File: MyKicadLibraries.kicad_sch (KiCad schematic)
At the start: 18 parts, among them J1 Conn_01x08, J2 Conn_01x08, J3 POGO Pins, J4 c8-inlet, J5 FTDI, SW1 Schurter Switch, U1 radio-receiver, U10 rdm-6300, U2 TP4056, U3 LilygoSIMT7000G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

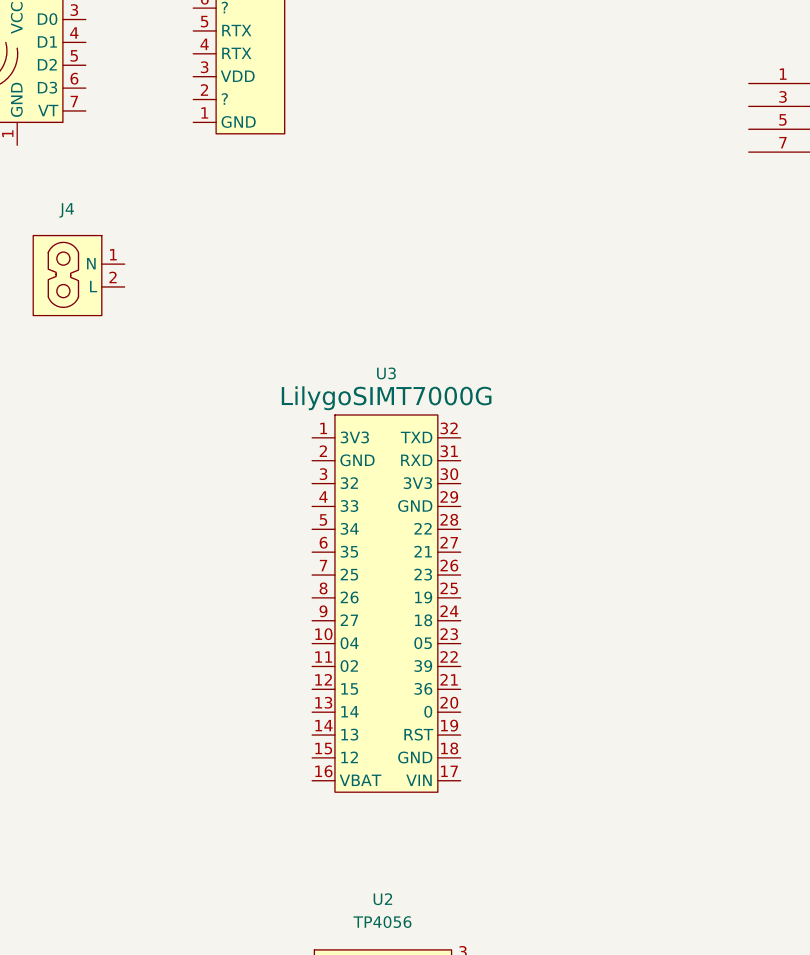
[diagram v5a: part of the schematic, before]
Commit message: add round magnetic charger and update the libraries
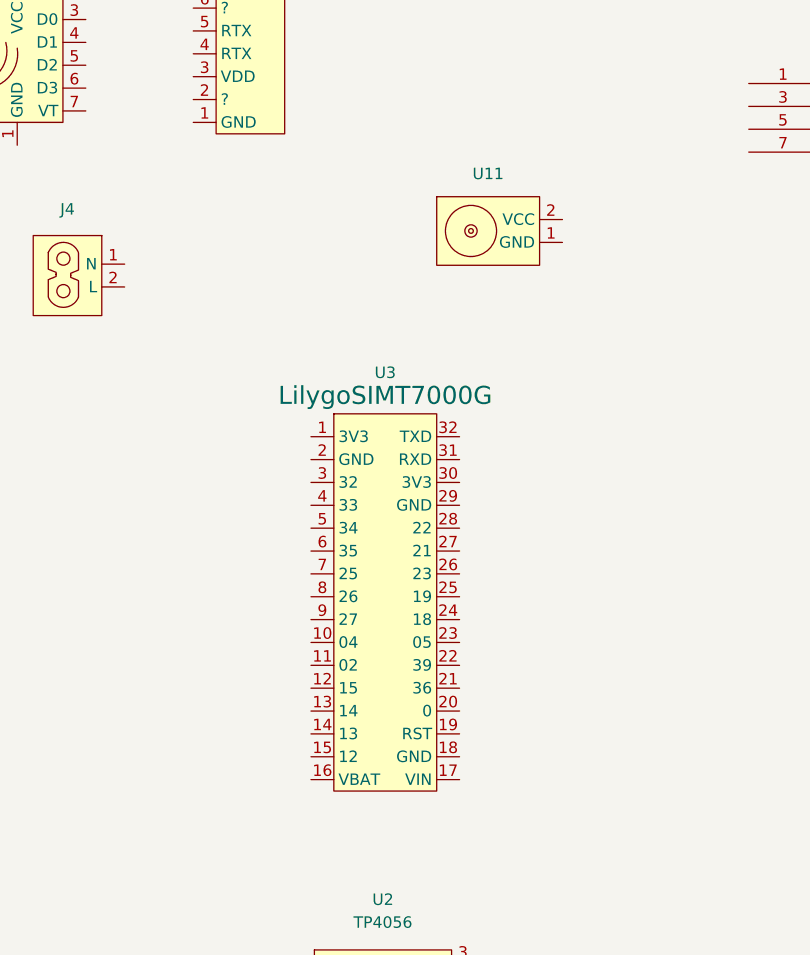
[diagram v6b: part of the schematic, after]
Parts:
- added U11: magnetic-charger, magnetic-charger:magnetic-charger, symbol magnetic-charger:magnetic-charger
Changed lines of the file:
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@@
+    (pin "2")
+  )
+  (symbol (lib_name "magnetic-charger_1") (lib_id "magnetic-charger:magnetic-charger") (at 141.605 71.755 0) (unit 1)
+    (in_bom yes) (on_board yes) (fields_autoplaced)
+    (property "Reference" "U11" (id 0) (at 140.97 65.405 0))
+    (property "Value" "magnetic-charger" (id 1) (at 140.97 76.835 0)
+      (effects (font (size 1.27 1.27)) hide)
+    )
+    (property "Footprint" "magnetic-charger:magnetic-charger" (id 2) (at 145.415 80.01 0)
+      (effects (font (size 1.27 1.27)) hide)
+    )
+    (property "Datasheet" "" (id 3) (at 146.685 72.39 0)
+      (effects (font (size 1.27 1.27)) hide)
+    )
+    (pin "1")
     (pin "2")
   )
@@
     (pin "4")
   )
-  (symbol (lib_id "LilygoSimT7000:LilygoSIMT7000G") (at 130.302 112.522 0) (unit 1)
-    (in_bom yes) (on_board yes) (fields_autoplaced)
-    (property "Reference" "U3" (id 0) (at 129.667 87.63 0))
-    (property "Value" "LilygoSIMT7000G" (id 1) (at 129.667 90.17 0)
+  (symbol (lib_id "LilygoSimT7000:LilygoSIMT7000G") (at 130.175 112.395 0) (unit 1)
+    (in_bom yes) (on_board yes) (fields_autoplaced)
+    (property "Reference" "U3" (id 0) (at 129.54 87.503 0))
+    (property "Value" "LilygoSIMT7000G" (id 1) (at 129.54 90.043 0)
       (effects (font (size 2 2)))
     )
-    (property "Footprint" "LilygoSimT7000:LilygoSIM7000G" (id 2) (at 130.302 90.932 0)
-      (effects (font (size 1.27 1.27)) hide)
-    )
-    (property "Datasheet" "" (id 3) (at 130.302 90.932 0)
+    (property "Footprint" "LilygoSimT7000:LilygoSIM7000G" (id 2) (at 130.175 90.805 0)
+      (effects (font (size 1.27 1.27)) hide)
+    )
+    (property "Datasheet" "" (id 3) (at 130.175 90.805 0)
       (effects (font (size 1.27 1.27)) hide)
     )
@@
       (reference "U10") (unit 1) (value "rdm-6300") (footprint "rdm-6300:rdm-6300")
     )
-  )
+    (path "/6ca18766-67e5-4cf7-b987-be25548a3c86"
+      (reference "U11") (unit 1) (value "magnetic-charger") (footprint "magnetic-charger:magnetic-charger")
+    )
+  )

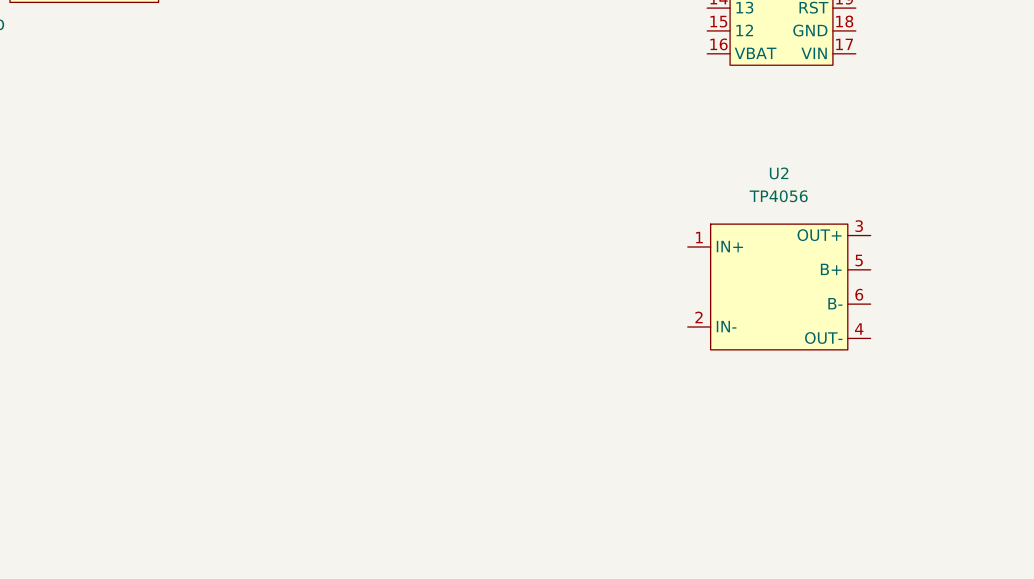
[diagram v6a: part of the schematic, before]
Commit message: Update magnetic charger plug and sd card module
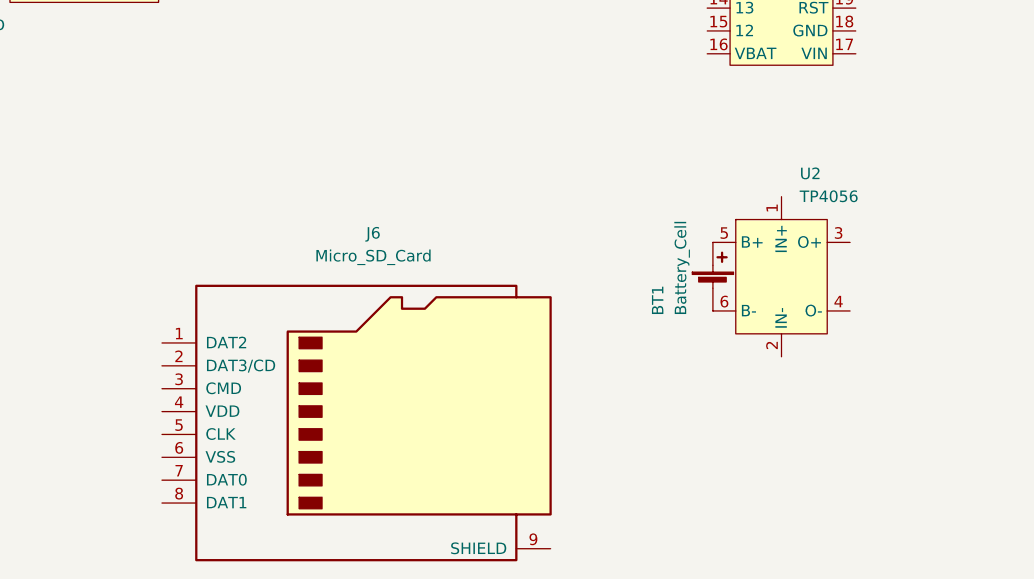
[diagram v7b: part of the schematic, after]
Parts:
- added BT1: Battery_Cell, symbol Device:Battery_Cell
- added J6: Micro_SD_Card, sd-card:sd-card, symbol Connector:Micro_SD_Card
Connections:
- net at U2.5 (B+): now also BT1.1 (+)
- net at U2.6 (B-): now also BT1.2 (-)
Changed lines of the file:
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@@
     (pin "1")
+  )
+  (symbol (lib_id "Device:Battery_Cell") (at 121.92 158.75 0) (unit 1)
+    (in_bom yes) (on_board yes)
+    (property "Reference" "BT1" (id 0) (at 115.824 161.798 90)
+      (effects (font (size 1.27 1.27)) (justify left))
+    )
+    (property "Value" "Battery_Cell" (id 1) (at 118.364 161.798 90)
+      (effects (font (size 1.27 1.27)) (justify left))
+    )
+    (property "Footprint" "" (id 2) (at 121.92 157.226 90)
+      (effects (font (size 1.27 1.27)) hide)
+    )
+    (property "Datasheet" "~" (id 3) (at 121.92 157.226 90)
+      (effects (font (size 1.27 1.27)) hide)
+    )
+    (pin "1")
+    (pin "2")
   )
   (symbol (lib_id "ftdi-connector:FTDI") (at 108.204 54.61 0) (unit 1)
@@
     (pin "7")
     (pin "8")
+  )
+  (symbol (lib_id "TP4056:TP4056") (at 129.54 157.48 0) (unit 1)
+    (in_bom yes) (on_board yes) (fields_autoplaced)
+    (property "Reference" "U2" (id 0) (at 131.5594 146.05 0)
+      (effects (font (size 1.27 1.27)) (justify left))
+    )
+    (property "Value" "TP4056" (id 1) (at 131.5594 148.59 0)
+      (effects (font (size 1.27 1.27)) (justify left))
+    )
+    (property "Footprint" "TP4056:TP4056" (id 2) (at 128.27 131.445 0)
+      (effects (font (size 1.27 1.27)) hide)
+    )
+    (property "Datasheet" "" (id 3) (at 128.27 131.445 0)
+      (effects (font (size 1.27 1.27)) hide)
+    )
+    (pin "1")
+    (pin "2")
+    (pin "3")
+    (pin "4")
+    (pin "5")
+    (pin "6")
+  )
+  (symbol (lib_id "Connector:Micro_SD_Card") (at 83.566 172.466 0) (unit 1)
+    (in_bom yes) (on_board yes) (fields_autoplaced)
+    (property "Reference" "J6" (id 0) (at 84.201 152.654 0))
+    (property "Value" "Micro_SD_Card" (id 1) (at 84.201 155.194 0))
+    (property "Footprint" "sd-card:sd-card" (id 2) (at 112.776 164.846 0)
+      (effects (font (size 1.27 1.27)) hide)
+    )
+    (property "Datasheet" "http://katalog.we-online.de/em/datasheet/693072010801.pdf" (id 3) (at 83.566 172.466 0)
+      (effects (font (size 1.27 1.27)) hide)
+    )
+    (pin "1")
+    (pin "2")
+    (pin "3")
+    (pin "4")
+    (pin "5")
+    (pin "6")
+    (pin "7")
+    (pin "8")
+    (pin "9")
   )
   (symbol (lib_id "neopixel-strip:LEDs_In") (at 29.21 43.18 0) (unit 1)
@@
     (pin "4")
   )
-  (symbol (lib_id "TP4056:TP4056") (at 129.286 159.258 0) (unit 1)
-    (in_bom yes) (on_board yes) (fields_autoplaced)
-    (property "Reference" "U2" (id 0) (at 129.286 146.05 0))
-    (property "Value" "TP4056" (id 1) (at 129.286 148.59 0))
-    (property "Footprint" "TP4056:TP4056" (id 2) (at 129.286 132.588 0)
-      (effects (font (size 1.27 1.27)) hide)
-    )
-    (property "Datasheet" "" (id 3) (at 129.286 132.588 0)
-      (effects (font (size 1.27 1.27)) hide)
-    )
-    (pin "1")
-    (pin "2")
-    (pin "3")
-    (pin "4")
-    (pin "5")
-    (pin "6")
-  )
   (symbol (lib_id "Connector_Generic:Conn_01x08") (at 212.725 135.255 0) (mirror y) (unit 1)
     (in_bom yes) (on_board yes) (fields_autoplaced)
@@
       (reference "#PWR0103") (unit 1) (value "GND") (footprint "")
     )
+    (path "/0cd8403f-406a-4eab-8a59-bcebc0593a4b"
+      (reference "BT1") (unit 1) (value "Battery_Cell") (footprint "")
+    )
     (path "/d968a578-d892-4ece-acfe-f95f8b4cdb95"
       (reference "J1") (unit 1) (value "Conn_01x08") (footprint "Connector_PinHeader_2.54mm:PinHeader_1x08_P2.54mm_Vertical")
@@
       (reference "J5") (unit 1) (value "FTDI") (footprint "Connector_PinHeader_2.54mm:PinHeader_1x06_P2.54mm_Horizontal")
     )
+    (path "/928cb1b4-1b49-47a7-a21b-69ee5b3fa19d"
+      (reference "J6") (unit 1) (value "Micro_SD_Card") (footprint "sd-card:sd-card")
+    )
     (path "/93625391-d5f1-4afc-86f7-69a3da3b5437"
       (reference "LIN1") (unit 1) (value "LEDs_In") (footprint "neopixel-strip:neopixel-strip")
@@
       (reference "U1") (unit 1) (value "radio-receiver") (footprint "radio-receiver:radio-receiver")
     )
-    (path "/d6c25bfa-6d1f-4054-a172-92157c1e1494"
+    (path "/8e4cc5f0-d50f-4454-b7ee-302278541603"
       (reference "U2") (unit 1) (value "TP4056") (footprint "TP4056:TP4056")
     )

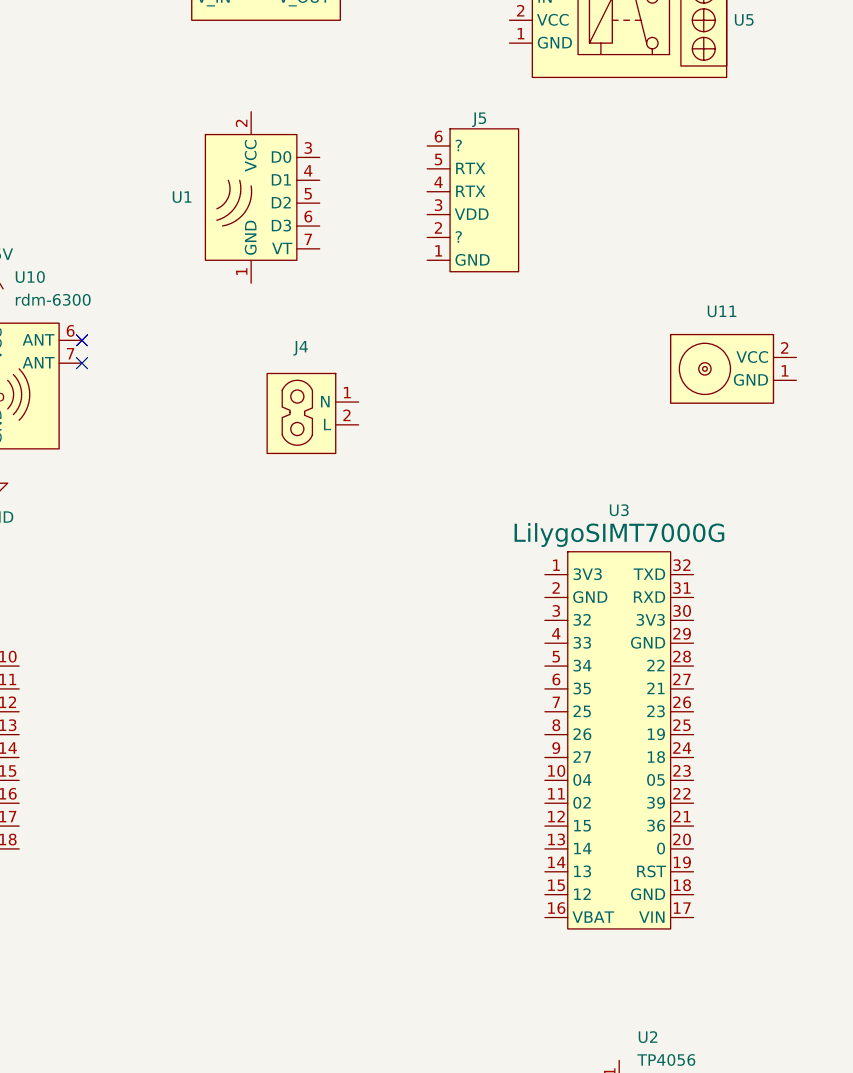
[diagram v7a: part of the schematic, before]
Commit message: Update TTL symbol
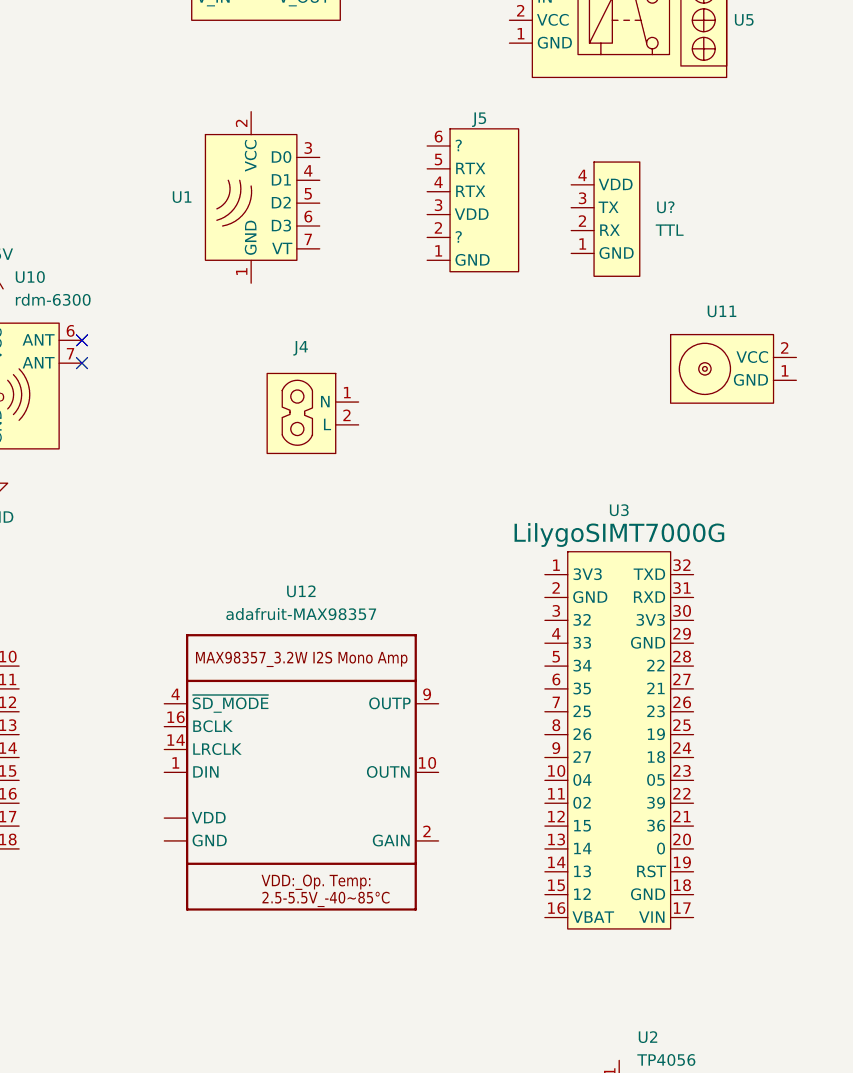
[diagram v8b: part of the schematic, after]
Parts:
- added U12: adafruit-MAX98357, adafruit-MAX98357:adafruit-MAX98357, symbol adafruit-MAX98357:adafruit-MAX98357
- added U?: TTL, Connector_PinHeader_2.54mm:PinHeader_1x04_P2.54mm_Vertical, symbol ftdi-connector:TTL
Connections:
- new net: U12.11 (GND), U12.15 (GND), U12.3 (GND), U12.THERMAL (GND)
- new net: U12.7 (VDD), U12.8 (VDD)
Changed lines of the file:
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@@
     (pin "3")
+  )
+  (symbol (lib_id "ftdi-connector:TTL") (at 126.746 53.848 0) (unit 1)
+    (in_bom yes) (on_board yes) (fields_autoplaced)
+    (property "Reference" "U?" (id 0) (at 133.604 53.8479 0)
+      (effects (font (size 1.27 1.27)) (justify left))
+    )
+    (property "Value" "TTL" (id 1) (at 133.604 56.3879 0)
+      (effects (font (size 1.27 1.27)) (justify left))
+    )
+    (property "Footprint" "Connector_PinHeader_2.54mm:PinHeader_1x04_P2.54mm_Vertical" (id 2) (at 129.286 66.548 0)
+      (effects (font (size 1.27 1.27)) hide)
+    )
+    (property "Datasheet" "" (id 3) (at 126.746 53.848 0)
+      (effects (font (size 1.27 1.27)) hide)
+    )
+    (pin "1")
+    (pin "2")
+    (pin "3")
+    (pin "4")
   )
   (symbol (lib_id "rdm-6300:rdm-6300") (at 60.325 73.66 0) (unit 1)
@@
     (pin "6")
     (pin "7")
+  )
+  (symbol (lib_id "adafruit-MAX98357:adafruit-MAX98357") (at 94.234 116.586 0) (unit 1)
+    (in_bom yes) (on_board yes) (fields_autoplaced)
+    (property "Reference" "U12" (id 0) (at 94.234 96.52 0))
+    (property "Value" "adafruit-MAX98357" (id 1) (at 94.234 99.06 0))
+    (property "Footprint" "adafruit-MAX98357:adafruit-MAX98357" (id 2) (at 97.409 136.271 0)
+      (effects (font (size 1.27 1.27)) hide)
+    )
+    (property "Datasheet" "" (id 3) (at 94.234 116.586 0)
+      (effects (font (size 1.27 1.27)) hide)
+    )
+    (pin "1")
+    (pin "10")
+    (pin "11")
+    (pin "14")
+    (pin "15")
+    (pin "16")
+    (pin "2")
+    (pin "3")
+    (pin "4")
+    (pin "7")
+    (pin "8")
+    (pin "9")
+    (pin "THERMAL")
   )
   (symbol (lib_id "Switch:SW_Push") (at 196.85 85.09 0) (unit 1)
@@
       (reference "U11") (unit 1) (value "magnetic-charger") (footprint "magnetic-charger:magnetic-charger")
     )
-  )
+    (path "/57891687-79ed-4f16-a621-bfebf267576c"
+      (reference "U12") (unit 1) (value "adafruit-MAX98357") (footprint "adafruit-MAX98357:adafruit-MAX98357")
+    )
+    (path "/435d2a60-6fae-43fe-9627-fd91fed8fe4a"
+      (reference "U?") (unit 1) (value "TTL") (footprint "Connector_PinHeader_2.54mm:PinHeader_1x04_P2.54mm_Vertical")
+    )
+  )
